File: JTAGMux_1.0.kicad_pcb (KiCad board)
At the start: 4 copper layers, 57.9 x 41.2 mm, 15 parts, among them J1 (Expension and configuration) Conn_02x10_Odd_Even, M1 MountingHole_3.7mm, M2 MountingHole_3.7mm, U1 SN74CBTLV16292DL

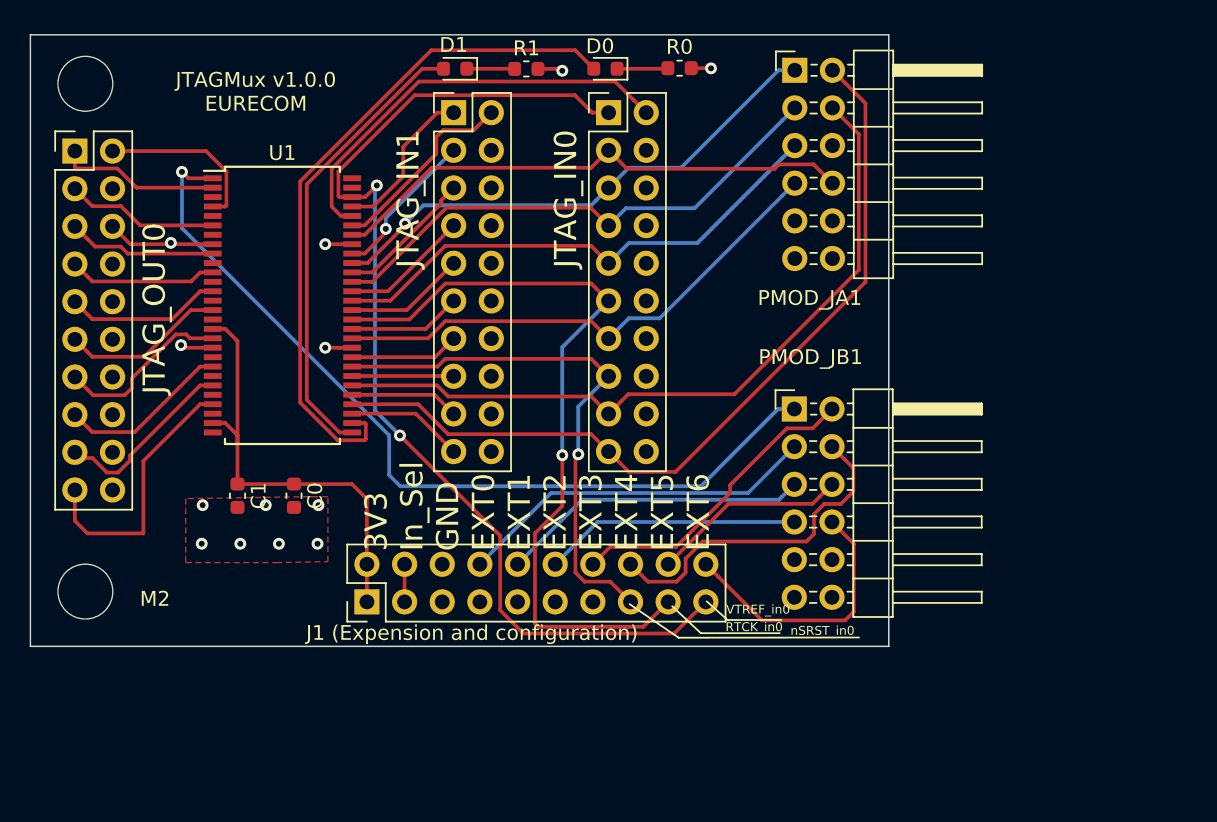
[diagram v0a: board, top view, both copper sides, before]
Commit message: minor routing improvement + adding pdf and gerber files
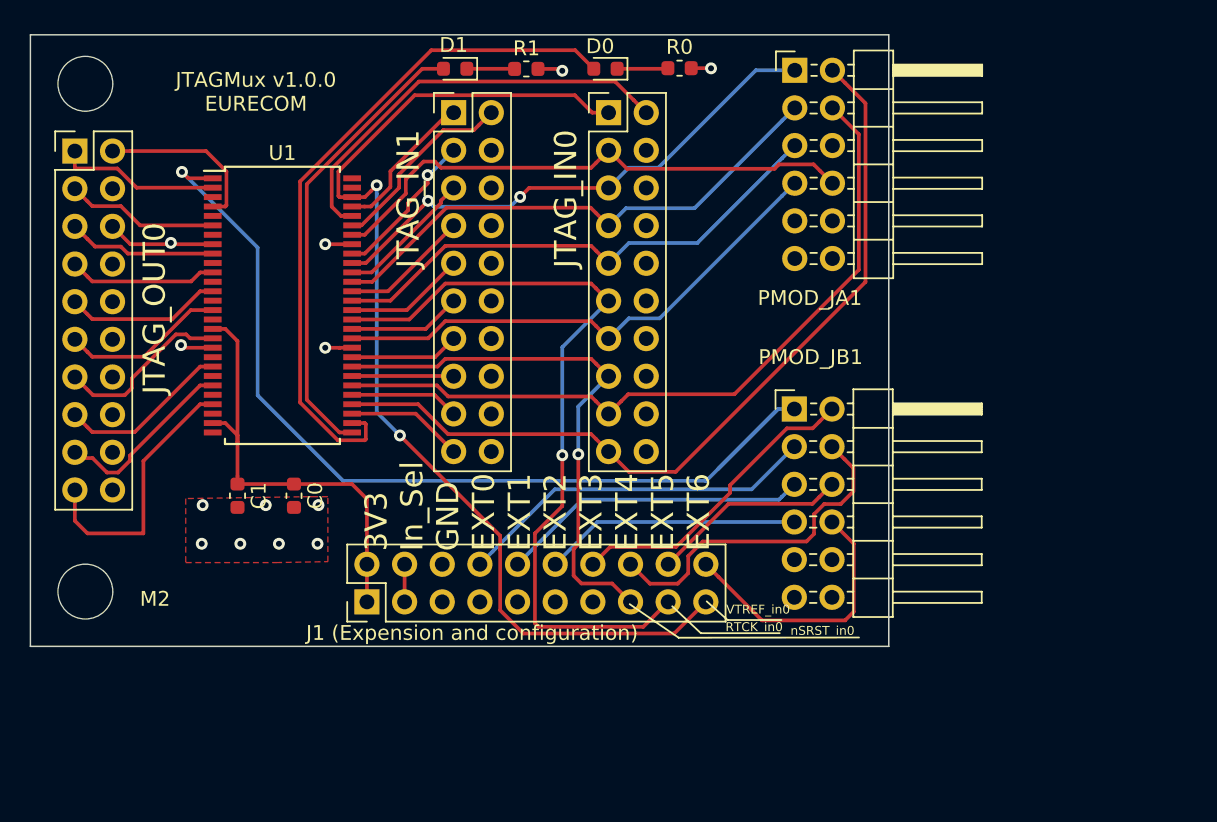
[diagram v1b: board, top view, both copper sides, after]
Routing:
- net Select_input: track 64.0 -> 65.8 mm
- net nTRST_in0: track 35.9 -> 36.8 mm
- net VTREF_in1: track 10.6 -> 10.1 mm
- net TDI_in0: track 35.3 -> 35.6 mm, vias 1 -> 2

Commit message: version 1.0.1
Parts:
- J1: renamed from J1 (Expension and configuration)
- moved M1 83.2 mm to (124.3, 156.0), turned to 180 degrees
- moved JTAG_OUT0 80.0 mm to (125.0, 151.5), turned to 180 degrees
- moved M2 74.6 mm to (124.3, 121.8), turned to 180 degrees
- moved C1 51.3 mm to (114.1, 128.3), turned to 90 degrees
- moved D1 50.5 mm to (99.4, 157.1), turned to 0 degrees
- moved R1 47.4 mm to (94.6, 157.1), turned to 180 degrees
- moved R0 47.2 mm to (84.3, 157.1), turned to 180 degrees
- moved U1 46.2 mm to (111.0, 141.1), turned to 180 degrees
- moved D0 46.1 mm to (89.3, 157.1), turned to 0 degrees
- moved JTAG_IN1 45.3 mm to (99.5, 154.1), turned to 180 degrees
- moved C0 43.9 mm to (110.3, 128.3), turned to 90 degrees
- moved J1 41.5 mm to (105.3, 121.1), turned to 270 degrees
- moved JTAG_IN0 40.2 mm to (89.0, 154.1), turned to 180 degrees
- moved PMOD_JA1 27.2 mm to (76.5, 121.4)
- moved PMOD_JB1 27.2 mm to (76.5, 144.2)
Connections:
- PMOD_JA1 pad 9: Net-(PMOD_JA1-Pad9) -> (no net)
- U1 pad 10: Net-(U1-Pad10) -> (no net)
- U1 pad 12: Net-(U1-Pad12) -> (no net)
- U1 pad 14: Net-(U1-Pad14) -> (no net)
- U1 pad 16: Net-(U1-Pad16) -> (no net)
- U1 pad 20: Net-(U1-Pad20) -> (no net)
- U1 pad 22: Net-(U1-Pad22) -> (no net)
- U1 pad 24: Net-(U1-Pad24) -> (no net)
- U1 pad 26: Net-(U1-Pad26) -> (no net)
- U1 pad 28: Net-(U1-Pad28) -> (no net)
- U1 pad 3: Net-(U1-Pad3) -> (no net)
- U1 pad 5: Net-(U1-Pad5) -> (no net)
- U1 pad 55: Net-(U1-Pad55) -> (no net)
- U1 pad 56: Net-(U1-Pad56) -> (no net)
- U1 pad 7: Net-(U1-Pad7) -> (no net)
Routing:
- net TDI_in0: track 35.6 -> 61.0 mm
- net TMS_in0: track 35.7 -> 56.6 mm
- net EXT2: track 17.3 -> 36.9 mm, vias 0 -> 1
- net EXT5: track 13.3 -> 31.7 mm
- net EXT1_IRQACK: track 20.9 -> 37.7 mm, vias 0 -> 1
- net EXT6: track 18.4 -> 33.5 mm
- net nTRST_in0: track 36.8 -> 51.7 mm
- net EXT0_IRQ: track 24.5 -> 38.0 mm, vias 0 -> 1
- net Select_input: track 65.8 -> 53.1 mm
- net DBACK_in0: track 57.0 -> 47.2 mm, vias 0 -> 1
- net TCK_in0: track 35.2 -> 45.0 mm
- net DBRQ_in0: track 50.7 -> 41.1 mm
- net EXT3: track 20.8 -> 29.6 mm
- net EXT4: track 23.2 -> 31.0 mm
- net DBACK_out: track 18.2 -> 15.4 mm
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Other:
- board text added: "JTAGMux v1.0.1 EURECOM"
- board text removed: "JTAGMux v1.0.0 EURECOM"

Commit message: Update to KiCad 8.0 with removal of rescue lefovers
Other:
- net class Default removed
